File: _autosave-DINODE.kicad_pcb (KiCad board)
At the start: 2 copper layers, 29 parts, among them J1 Barrel_Jack, J10 Conn_01x03_Male, J11 Conn_02x04_Odd_Even, J2 Conn_01x02_Male, J3 Conn_01x07, J4 Conn_01x16, J5 Conn_02x04_Odd_Even, J6 Conn_02x04_Odd_Even, J7 Conn_02x04_Odd_Even, J9 Conn_02x04_Odd_Even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

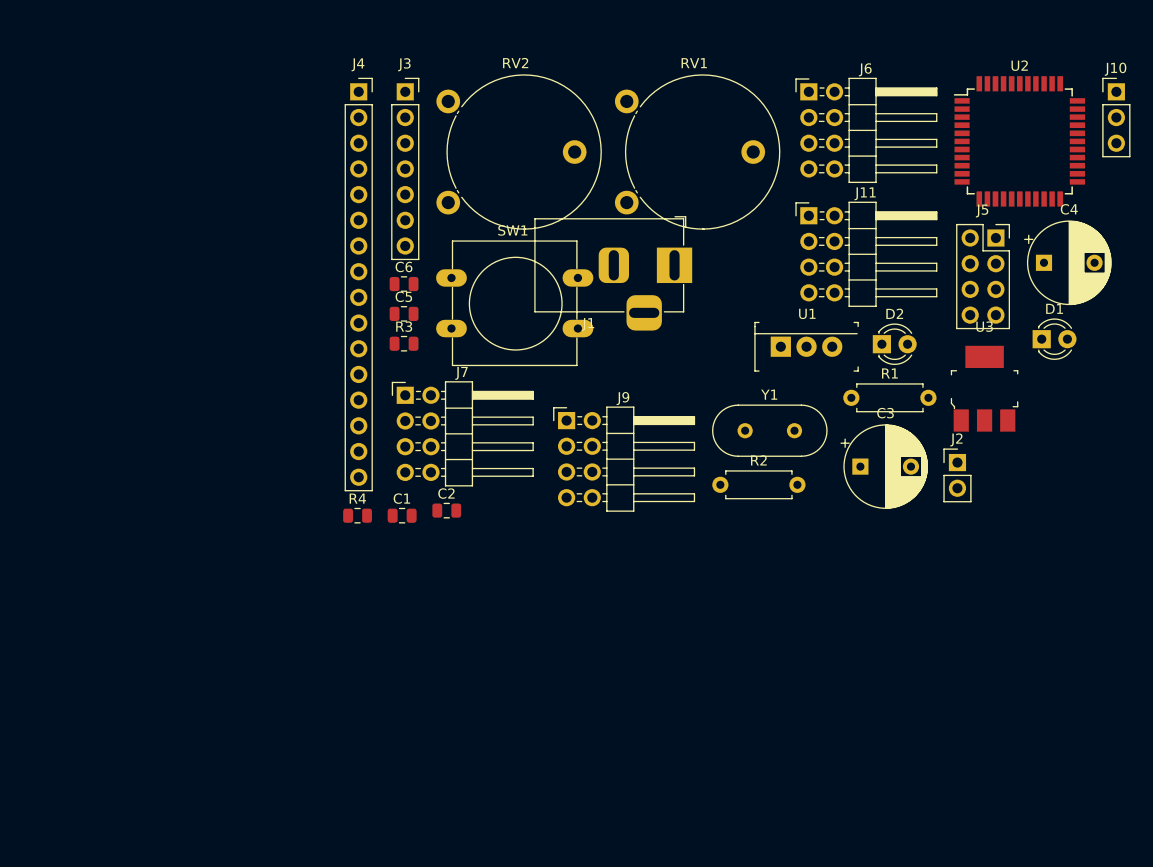
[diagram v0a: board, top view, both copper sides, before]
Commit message: Updated circuit footprints
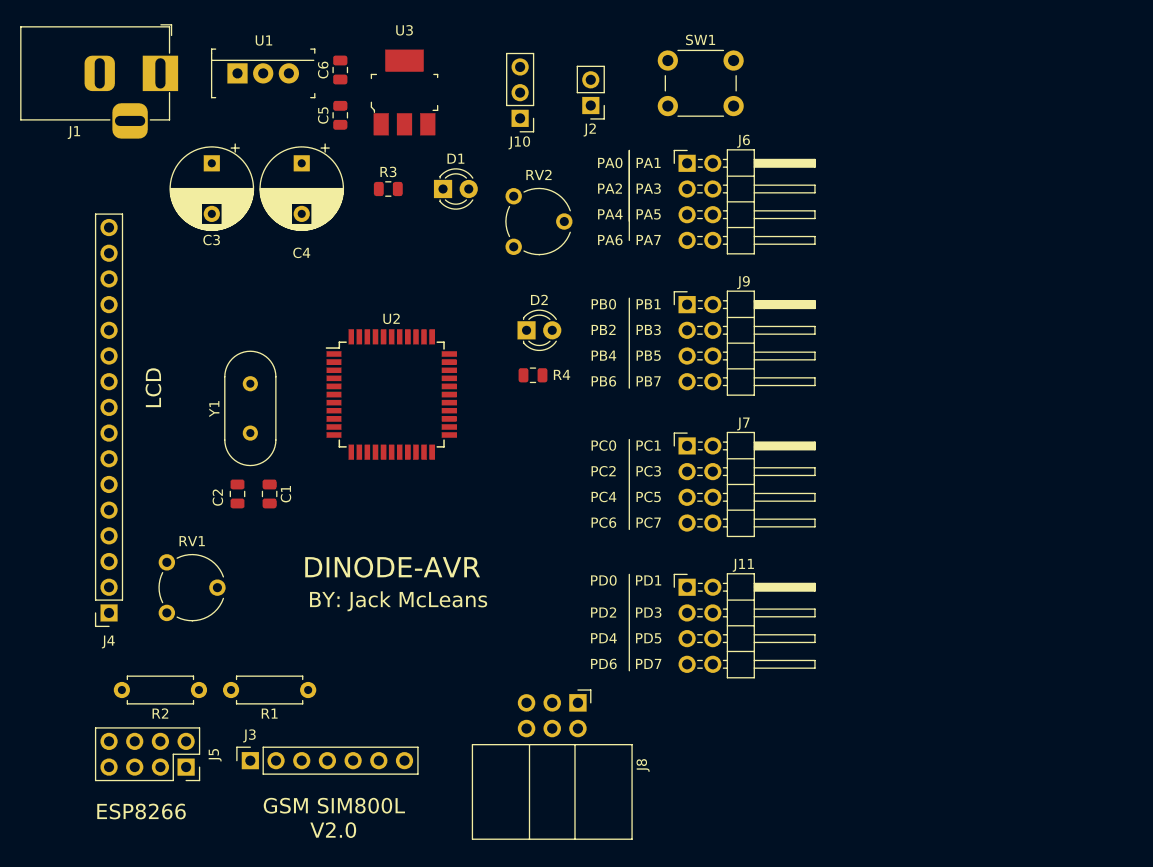
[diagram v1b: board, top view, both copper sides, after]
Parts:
- added J8: AVR-ISP-6, Connector_IDC:IDC-Header_2x03_P2.54mm_Horizontal, F.Cu at (141.6, 115.6)
- RV1, RV2: footprint Potentiometer_THT:Potentiometer_Piher_PT-15-V02_Vertical -> Potentiometer_THT:Potentiometer_Piher_PT-6-V_Vertical
- SW1: footprint Button_Switch_THT:SW_PUSH-12mm -> Button_Switch_THT:SW_PUSH_6mm_H4.3mm
- moved J5 95.6 mm to (102.9, 121.9), turned to 270 degrees
- moved C4 74.0 mm to (114.3, 62.2), turned to 270 degrees
- moved C3 70.8 mm to (105.4, 62.2), turned to 270 degrees
- moved J3 67.9 mm to (109.2, 121.3), turned to 90 degrees
- moved U2 66.9 mm to (123.2, 85.1)
- moved U3 64.4 mm to (124.5, 55.2)
- moved D1 61.0 mm to (128.3, 64.8)
- moved R1 61.0 mm to (114.9, 114.3), turned to 180 degrees
- moved RV1 60.9 mm to (101.0, 106.7)
- moved U1 60.1 mm to (108.0, 53.3)
- moved J10 59.0 mm to (135.9, 57.8), turned to 180 degrees
- moved J4 57.1 mm to (95.2, 106.7), turned to 180 degrees
- moved R2 55.4 mm to (104.1, 114.3), turned to 180 degrees
- moved J1 54.3 mm to (100.3, 53.3)
- moved J2 50.6 mm to (142.9, 56.5), turned to 180 degrees
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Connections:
- C4 pad 1: RESET -> +5V
- C6 pad 1: RESET -> +5V
- D1 pad 2: RESET -> +5V
- J10 pad 3: RESET -> +5V
- J2 pad 2: RESET -> +5V
- J3 pad 1: RESET -> +5V
- J4 pad 15: RESET -> +5V
- J4 pad 2: RESET -> +5V
- J5 pad 1: ESP_RX -> GND
- J5 pad 2: +3V3 -> PD_0
- J5 pad 4: Net-(J5-Pad4) -> +3V3
- J5 pad 6: +3V3 -> Net-(J5-Pad6)
- J5 pad 7: GND -> ESP_RX
- J5 pad 8: PD_0 -> +3V3
- RV1 pad 3: RESET -> +5V
- RV2 pad 3: RESET -> +5V
- SW1 pad 2: RESET -> Net-(SW1-Pad2)
- U1 pad 3: RESET -> +5V
- U2 pad 17: RESET -> +5V
- U2 pad 38: RESET -> +5V
- U2 pad 4: RESET -> Net-(SW1-Pad2)
- U2 pad 5: RESET -> +5V
- U3 pad 3: RESET -> +5V
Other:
- board text added: "BY: Jack McLeans"
- board text added: "DINODE-AVR"
- board text added: "ESP8266"
- board text added: "GSM SIM800L V2.0"
- board text added: "LCD"
- board text added: "PA0"
- board text added: "PA1"
- board text added: "PA2"
- board text added: "PA3"
- board text added: "PA4"
- board text added: "PA5"
- board text added: "PA6"
- board text added: "PA7"
- board text added: "PB0"
- board text added: "PB1"
- board text added: "PB2"
- board text added: "PB3"
- board text added: "PB4"
- board text added: "PB5"
- board text added: "PB6"
- board text added: "PB7"
- board text added: "PC0"
- board text added: "PC1"
- board text added: "PC2"
- board text added: "PC3"
- board text added: "PC4"
- board text added: "PC5"
- board text added: "PC6"
- board text added: "PC7"
- board text added: "PD0"
- board text added: "PD1"
- board text added: "PD2"
- board text added: "PD3"
- board text added: "PD4"
- board text added: "PD5"
- board text added: "PD6"
- board text added: "PD7"
